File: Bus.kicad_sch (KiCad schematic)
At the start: 8 parts, among them X1.1 BUS_EC1834_16Bit, X1.2 BUS_EC1834_16Bit, X1.3 BUS_EC1834_16Bit, X1.4 BUS_EC1834_16Bit, X1.5 BUS_EC1834_16Bit, X1.6 BUS_EC1834_16Bit, X1.7 BUS_EC1834_16Bit, X1.8 BUS_EC1834_16Bit

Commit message: Completed BUS Final checks required
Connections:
- net GND: now reaches X1.2.a1 (GND)
- net GND: now also X1.1.a1 (GND), X1.1.a10 (GND), X1.1.a31 (GND), X1.1.a32 (GND), X1.2.a10 (GND), X1.2.a31 (GND), X1.2.a32 (GND), X1.3.a1 (GND), X1.3.a10 (GND), X1.3.a31 (GND), X1.3.a32 (GND), X1.4.a1 (GND), X1.4.a10 (GND), X1.4.a31 (GND), X1.4.a32 (GND), X1.5.a1 (GND), X1.5.a10 (GND), X1.5.a31 (GND), X1.5.a32 (GND), X1.6.a1 (GND), X1.6.a10 (GND), X1.6.a31 (GND), X1.6.a32 (GND), X1.7.a1 (GND), X1.7.a10 (GND), X1.7.a31 (GND), X1.7.a32 (GND), X1.8.a1 (GND), X1.8.a10 (GND), X1.8.a31 (GND), X1.8.a32 (GND)
- net ~{MEMW}: now reaches X1.2.a11 (~{MEMW})
- net ~{MEMW}: now also X1.1.a11 (~{MEMW}), X1.3.a11 (~{MEMW}), X1.4.a11 (~{MEMW}), X1.5.a11 (~{MEMW}), X1.6.a11 (~{MEMW}), X1.7.a11 (~{MEMW}), X1.8.a11 (~{MEMW})
- net ~{MEMR}: now reaches X1.2.a12 (~{MEMR})
- net ~{MEMR}: now also X1.1.a12 (~{MEMR}), X1.3.a12 (~{MEMR}), X1.4.a12 (~{MEMR}), X1.5.a12 (~{MEMR}), X1.6.a12 (~{MEMR}), X1.7.a12 (~{MEMR}), X1.8.a12 (~{MEMR})
- net ~{IOW}: now reaches X1.2.a13 (~{IOW})
- net ~{IOW}: now also X1.1.a13 (~{IOW}), X1.3.a13 (~{IOW}), X1.4.a13 (~{IOW}), X1.5.a13 (~{IOW}), X1.6.a13 (~{IOW}), X1.7.a13 (~{IOW}), X1.8.a13 (~{IOW})
- net ~{IOR}: now reaches X1.2.a14 (~{IOR})
- net ~{IOR}: now also X1.1.a14 (~{IOR}), X1.3.a14 (~{IOR}), X1.4.a14 (~{IOR}), X1.5.a14 (~{IOR}), X1.6.a14 (~{IOR}), X1.7.a14 (~{IOR}), X1.8.a14 (~{IOR})
- net ~{DACK3}: now reaches X1.2.a15 (~{DACK3})
- net ~{DACK3}: now also X1.1.a15 (~{DACK3}), X1.3.a15 (~{DACK3}), X1.4.a15 (~{DACK3}), X1.5.a15 (~{DACK3}), X1.6.a15 (~{DACK3}), X1.7.a15 (~{DACK3}), X1.8.a15 (~{DACK3})
- net DRQ3: now reaches X1.2.a16 (DRQ3)
- net DRQ3: now also X1.1.a16 (DRQ3), X1.3.a16 (DRQ3), X1.4.a16 (DRQ3), X1.5.a16 (DRQ3), X1.6.a16 (DRQ3), X1.7.a16 (DRQ3), X1.8.a16 (DRQ3)
- net ~{DACK1}: now reaches X1.2.a17 (~{DACK1})
- net ~{DACK1}: now also X1.1.a17 (~{DACK1}), X1.3.a17 (~{DACK1}), X1.4.a17 (~{DACK1}), X1.5.a17 (~{DACK1}), X1.6.a17 (~{DACK1}), X1.7.a17 (~{DACK1}), X1.8.a17 (~{DACK1})
- net DRQ1: now reaches X1.2.a18 (DRQ1)
- net DRQ1: now also X1.1.a18 (DRQ1), X1.3.a18 (DRQ1), X1.4.a18 (DRQ1), X1.5.a18 (DRQ1), X1.6.a18 (DRQ1), X1.7.a18 (DRQ1), X1.8.a18 (DRQ1)
- net ~{DACK0}: now reaches X1.2.a19 (~{DACK0})
- net ~{DACK0}: now also X1.1.a19 (~{DACK0}), X1.3.a19 (~{DACK0}), X1.4.a19 (~{DACK0}), X1.5.a19 (~{DACK0}), X1.6.a19 (~{DACK0}), X1.7.a19 (~{DACK0}), X1.8.a19 (~{DACK0})
- net RESET: now reaches X1.2.a2 (RESET)
- net RESET: now also X1.1.a2 (RESET), X1.3.a2 (RESET), X1.4.a2 (RESET), X1.5.a2 (RESET), X1.6.a2 (RESET), X1.7.a2 (RESET), X1.8.a2 (RESET)
- net CLK: now reaches X1.2.a20 (CLK)
- net CLK: now also X1.1.a20 (CLK), X1.3.a20 (CLK), X1.4.a20 (CLK), X1.5.a20 (CLK), X1.6.a20 (CLK), X1.7.a20 (CLK), X1.8.a20 (CLK)
- net IRQ7: now reaches X1.2.a21 (IRQ7)
- net IRQ7: now also X1.1.a21 (IRQ7), X1.3.a21 (IRQ7), X1.4.a21 (IRQ7), X1.5.a21 (IRQ7), X1.6.a21 (IRQ7), X1.7.a21 (IRQ7), X1.8.a21 (IRQ7)
- net IRQ6: now reaches X1.2.a22 (IRQ6)
- net IRQ6: now also X1.1.a22 (IRQ6), X1.3.a22 (IRQ6), X1.4.a22 (IRQ6), X1.5.a22 (IRQ6), X1.6.a22 (IRQ6), X1.7.a22 (IRQ6), X1.8.a22 (IRQ6)
- net IRQ5: now reaches X1.2.a23 (IRQ5)
- net IRQ5: now also X1.1.a23 (IRQ5), X1.3.a23 (IRQ5), X1.4.a23 (IRQ5), X1.5.a23 (IRQ5), X1.6.a23 (IRQ5), X1.7.a23 (IRQ5), X1.8.a23 (IRQ5)
- net IRQ4: now reaches X1.2.a24 (IRQ4)
- net IRQ4: now also X1.1.a24 (IRQ4), X1.3.a24 (IRQ4), X1.4.a24 (IRQ4), X1.5.a24 (IRQ4), X1.6.a24 (IRQ4), X1.7.a24 (IRQ4), X1.8.a24 (IRQ4)
- net IRQ3: now reaches X1.2.a25 (IRQ3)
- net IRQ3: now also X1.1.a25 (IRQ3), X1.3.a25 (IRQ3), X1.4.a25 (IRQ3), X1.5.a25 (IRQ3), X1.6.a25 (IRQ3), X1.7.a25 (IRQ3), X1.8.a25 (IRQ3)
- net ~{DACK2}: now reaches X1.2.a26 (~{DACK2})
- net ~{DACK2}: now also X1.1.a26 (~{DACK2}), X1.3.a26 (~{DACK2}), X1.4.a26 (~{DACK2}), X1.5.a26 (~{DACK2}), X1.6.a26 (~{DACK2}), X1.7.a26 (~{DACK2}), X1.8.a26 (~{DACK2})
- net TC: now reaches X1.2.a27 (TC)
- net TC: now also X1.1.a27 (TC), X1.3.a27 (TC), X1.4.a27 (TC), X1.5.a27 (TC), X1.6.a27 (TC), X1.7.a27 (TC), X1.8.a27 (TC)
- net ALE: now reaches X1.2.a28 (ALE)
- net ALE: now also X1.1.a28 (ALE), X1.3.a28 (ALE), X1.4.a28 (ALE), X1.5.a28 (ALE), X1.6.a28 (ALE), X1.7.a28 (ALE), X1.8.a28 (ALE)
- net +5V: now reaches X1.2.a29 (VCC)
- net +5V: now also X1.1.a29 (VCC), X1.1.a3 (+5V), X1.1.b30 (+5V), X1.2.a3 (+5V), X1.2.b30 (+5V), X1.3.a29 (VCC), X1.3.a3 (+5V), X1.3.b30 (+5V), X1.4.a29 (VCC), X1.4.a3 (+5V), X1.4.b30 (+5V), X1.5.a29 (VCC), X1.5.a3 (+5V), X1.5.b30 (+5V), X1.6.a29 (VCC), X1.6.a3 (+5V), X1.6.b30 (+5V), X1.7.a29 (VCC), X1.7.a3 (+5V), X1.7.b30 (+5V), X1.8.a29 (VCC), X1.8.a3 (+5V), X1.8.b30 (+5V)
- net OSC: now reaches X1.2.a30 (OSC)
- net OSC: now also X1.1.a30 (OSC), X1.3.a30 (OSC), X1.4.a30 (OSC), X1.5.a30 (OSC), X1.6.a30 (OSC), X1.7.a30 (OSC), X1.8.a30 (OSC)
- net IRQ2: now reaches X1.2.a4 (IRQ2)
- net IRQ2: now also X1.1.a4 (IRQ2), X1.3.a4 (IRQ2), X1.4.a4 (IRQ2), X1.5.a4 (IRQ2), X1.6.a4 (IRQ2), X1.7.a4 (IRQ2), X1.8.a4 (IRQ2)
- net -5V: now reaches X1.2.a5 (-5V)
- net -5V: now also X1.1.a5 (-5V), X1.3.a5 (-5V), X1.4.a5 (-5V), X1.5.a5 (-5V), X1.6.a5 (-5V), X1.7.a5 (-5V), X1.8.a5 (-5V)
- net DRQ2: now reaches X1.2.a6 (DRQ2)
- net DRQ2: now also X1.1.a6 (DRQ2), X1.3.a6 (DRQ2), X1.4.a6 (DRQ2), X1.5.a6 (DRQ2), X1.6.a6 (DRQ2), X1.7.a6 (DRQ2), X1.8.a6 (DRQ2)
- net -12V: now reaches X1.2.a7 (-12V)
- net -12V: now also X1.1.a7 (-12V), X1.3.a7 (-12V), X1.4.a7 (-12V), X1.5.a7 (-12V), X1.6.a7 (-12V), X1.7.a7 (-12V), X1.8.a7 (-12V)
- net +12V: now reaches X1.2.a9 (+12V)
- net +12V: now also X1.1.a9 (+12V), X1.3.a9 (+12V), X1.4.a9 (+12V), X1.5.a9 (+12V), X1.6.a9 (+12V), X1.7.a9 (+12V), X1.8.a9 (+12V)
- net DRQ0: now reaches X1.2.b19 (DRQ0)
- net DRQ0: now also X1.1.b19 (DRQ0), X1.3.b19 (DRQ0), X1.4.b19 (DRQ0), X1.5.b19 (DRQ0), X1.6.b19 (DRQ0), X1.7.b19 (DRQ0), X1.8.b19 (DRQ0)
- net IRQ10: now reaches X1.2.b21 (IRQ10)
- net IRQ10: now also X1.1.b21 (IRQ10), X1.3.b21 (IRQ10), X1.4.b21 (IRQ10), X1.5.b21 (IRQ10), X1.6.b21 (IRQ10), X1.7.b21 (IRQ10), X1.8.b21 (IRQ10)
- net IRQ11: now reaches X1.2.b22 (IRQ11)
- net IRQ11: now also X1.1.b22 (IRQ11), X1.3.b22 (IRQ11), X1.4.b22 (IRQ11), X1.5.b22 (IRQ11), X1.6.b22 (IRQ11), X1.7.b22 (IRQ11), X1.8.b22 (IRQ11)
- net IRQ12: now reaches X1.2.b23 (IRQ12)
- net IRQ12: now also X1.1.b23 (IRQ12), X1.3.b23 (IRQ12), X1.4.b23 (IRQ12), X1.5.b23 (IRQ12), X1.6.b23 (IRQ12), X1.7.b23 (IRQ12), X1.8.b23 (IRQ12)
- net IRQ15: now reaches X1.2.b24 (IRQ15)
- net IRQ15: now also X1.1.b24 (IRQ15), X1.3.b24 (IRQ15), X1.4.b24 (IRQ15), X1.5.b24 (IRQ15), X1.6.b24 (IRQ15), X1.7.b24 (IRQ15), X1.8.b24 (IRQ15)
- net IRQ14: now reaches X1.2.b25 (IRQ14)
- net IRQ14: now also X1.1.b25 (IRQ14), X1.3.b25 (IRQ14), X1.4.b25 (IRQ14), X1.5.b25 (IRQ14), X1.6.b25 (IRQ14), X1.7.b25 (IRQ14), X1.8.b25 (IRQ14)
- net ~{MASTER}: now reaches X1.2.b26 (~{MASTER})
- net ~{MASTER}: now also X1.1.b26 (~{MASTER}), X1.3.b26 (~{MASTER}), X1.4.b26 (~{MASTER}), X1.5.b26 (~{MASTER}), X1.6.b26 (~{MASTER}), X1.7.b26 (~{MASTER}), X1.8.b26 (~{MASTER})
- net ~{MEMCS16}: now reaches X1.2.b32 (~{MEMCS16})
- net ~{MEMCS16}: now also X1.1.b32 (~{MEMCS16}), X1.3.b32 (~{MEMCS16}), X1.4.b32 (~{MEMCS16}), X1.5.b32 (~{MEMCS16}), X1.6.b32 (~{MEMCS16}), X1.7.b32 (~{MEMCS16}), X1.8.b32 (~{MEMCS16})
- net ~{IOCHCK}: now reaches X1.2.c1 (~{IOCHCK})
- net ~{IOCHCK}: now also X1.1.c1 (~{IOCHCK}), X1.3.c1 (~{IOCHCK}), X1.4.c1 (~{IOCHCK}), X1.5.c1 (~{IOCHCK}), X1.6.c1 (~{IOCHCK}), X1.7.c1 (~{IOCHCK}), X1.8.c1 (~{IOCHCK})
- net IOCHRDY: now reaches X1.2.c10 (IOCHRDY)
- net IOCHRDY: now also X1.1.c10 (IOCHRDY), X1.3.c10 (IOCHRDY), X1.4.c10 (IOCHRDY), X1.5.c10 (IOCHRDY), X1.6.c10 (IOCHRDY), X1.7.c10 (IOCHRDY), X1.8.c10 (IOCHRDY)
- net AEN: now reaches X1.2.c11 (AEN)
- net AEN: now also X1.1.c11 (AEN), X1.3.c11 (AEN), X1.4.c11 (AEN), X1.5.c11 (AEN), X1.6.c11 (AEN), X1.7.c11 (AEN), X1.8.c11 (AEN)
- net A19: now reaches X1.2.c12 (BA19)
- net A19: now also X1.1.c12 (BA19), X1.4.c12 (BA19), X1.5.c12 (BA19), X1.6.c12 (BA19), X1.7.c12 (BA19), X1.8.c12 (BA19)
- net A18: now reaches X1.2.c13 (BA18)
- net A18: now also X1.1.c13 (BA18), X1.4.c13 (BA18), X1.5.c13 (BA18), X1.6.c13 (BA18), X1.7.c13 (BA18), X1.8.c13 (BA18)
- net A17: now reaches X1.2.c14 (BA17)
- net A17: now also X1.1.c14 (BA17), X1.4.c14 (BA17), X1.5.c14 (BA17), X1.6.c14 (BA17), X1.7.c14 (BA17), X1.8.c14 (BA17)
- net A16: now reaches X1.2.c15 (BA16)
- net A16: now also X1.1.c15 (BA16), X1.4.c15 (BA16), X1.5.c15 (BA16), X1.6.c15 (BA16), X1.7.c15 (BA16), X1.8.c15 (BA16)
- net A15: now reaches X1.2.c16 (BA15)
- net A15: now also X1.1.c16 (BA15), X1.4.c16 (BA15), X1.5.c16 (BA15), X1.6.c16 (BA15), X1.7.c16 (BA15), X1.8.c16 (BA15)
- net A14: now reaches X1.2.c17 (BA14)
- net A14: now also X1.1.c17 (BA14), X1.4.c17 (BA14), X1.5.c17 (BA14), X1.6.c17 (BA14), X1.7.c17 (BA14), X1.8.c17 (BA14)
- net A13: now reaches X1.2.c18 (BA13)
- net A13: now also X1.1.c18 (BA13), X1.4.c18 (BA13), X1.5.c18 (BA13), X1.6.c18 (BA13), X1.7.c18 (BA13), X1.8.c18 (BA13)
- net A12: now reaches X1.2.c19 (BA12)
- net A12: now also X1.1.c19 (BA12), X1.4.c19 (BA12), X1.5.c19 (BA12), X1.6.c19 (BA12), X1.7.c19 (BA12), X1.8.c19 (BA12)
- net D7: now reaches X1.2.c2 (DB7)
- net D7: now also X1.1.c2 (DB7), X1.3.c2 (DB7), X1.4.c2 (DB7), X1.5.c2 (DB7), X1.7.c2 (DB7), X1.8.c2 (DB7)
- net A11: now reaches X1.2.c20 (BA11)
- net A11: now also X1.1.c20 (BA11), X1.4.c20 (BA11), X1.5.c20 (BA11), X1.6.c20 (BA11), X1.7.c20 (BA11), X1.8.c20 (BA11)
- net A10: now reaches X1.2.c21 (BA10)
- net A10: now also X1.1.c21 (BA10), X1.4.c21 (BA10), X1.5.c21 (BA10), X1.6.c21 (BA10), X1.7.c21 (BA10), X1.8.c21 (BA10)
- net A9: now reaches X1.2.c22 (BA09)
- net A9: now also X1.1.c22 (BA09), X1.4.c22 (BA09), X1.5.c22 (BA09), X1.6.c22 (BA09), X1.7.c22 (BA09), X1.8.c22 (BA09)
- net A8: now reaches X1.2.c23 (BA08)
- net A8: now also X1.1.c23 (BA08), X1.4.c23 (BA08), X1.5.c23 (BA08), X1.6.c23 (BA08), X1.7.c23 (BA08), X1.8.c23 (BA08)
- net A7: now reaches X1.2.c24 (BA07)
- net A7: now also X1.1.c24 (BA07), X1.4.c24 (BA07), X1.5.c24 (BA07), X1.6.c24 (BA07), X1.7.c24 (BA07), X1.8.c24 (BA07)
- net A6: now reaches X1.2.c25 (BA06)
- net A6: now also X1.1.c25 (BA06), X1.4.c25 (BA06), X1.5.c25 (BA06), X1.6.c25 (BA06), X1.7.c25 (BA06), X1.8.c25 (BA06)
- net A5: now reaches X1.2.c26 (BA05)
- net A5: now also X1.1.c26 (BA05), X1.4.c26 (BA05), X1.5.c26 (BA05), X1.6.c26 (BA05), X1.7.c26 (BA05), X1.8.c26 (BA05)
- net A4: now reaches X1.2.c27 (BA04)
- net A4: now also X1.1.c27 (BA04), X1.4.c27 (BA04), X1.5.c27 (BA04), X1.6.c27 (BA04), X1.7.c27 (BA04), X1.8.c27 (BA04)
- net A3: now reaches X1.2.c28 (BA03)
- net A3: now also X1.1.c28 (BA03), X1.4.c28 (BA03), X1.5.c28 (BA03), X1.6.c28 (BA03), X1.7.c28 (BA03), X1.8.c28 (BA03)
- net A2: now reaches X1.2.c29 (BA02)
- net A2: now also X1.1.c29 (BA02), X1.4.c29 (BA02), X1.5.c29 (BA02), X1.6.c29 (BA02), X1.7.c29 (BA02), X1.8.c29 (BA02)
- net D6: now reaches X1.2.c3 (DB6)
- net D6: now also X1.1.c3 (DB6), X1.3.c3 (DB6), X1.4.c3 (DB6), X1.5.c3 (DB6), X1.7.c3 (DB6), X1.8.c3 (DB6)
- net A1: now reaches X1.2.c30 (BA01)
- net A1: now also X1.1.c30 (BA01), X1.4.c30 (BA01), X1.5.c30 (BA01), X1.6.c30 (BA01), X1.7.c30 (BA01), X1.8.c30 (BA01)
- net A0: now reaches X1.2.c31 (BA00)
- net A0: now also X1.1.c31 (BA00), X1.4.c31 (BA00), X1.5.c31 (BA00), X1.6.c31 (BA00), X1.7.c31 (BA00), X1.8.c31 (BA00)
- net ~{BHE}: now reaches X1.2.c32 (~{BHE})
- net ~{BHE}: now also X1.1.c32 (~{BHE}), X1.3.c32 (~{BHE}), X1.4.c32 (~{BHE}), X1.5.c32 (~{BHE}), X1.6.c32 (~{BHE}), X1.7.c32 (~{BHE}), X1.8.c32 (~{BHE})
- net D5: now reaches X1.2.c4 (DB5)
- net D5: now also X1.1.c4 (DB5), X1.3.c4 (DB5), X1.4.c4 (DB5), X1.5.c4 (DB5), X1.7.c4 (DB5), X1.8.c4 (DB5)
- net D4: now reaches X1.2.c5 (DB4)
- net D4: now also X1.1.c5 (DB4), X1.3.c5 (DB4), X1.4.c5 (DB4), X1.5.c5 (DB4), X1.6.c5 (DB4), X1.7.c5 (DB4), X1.8.c5 (DB4)
- net D3: now reaches X1.2.c6 (DB3)
- net D3: now also X1.1.c6 (DB3), X1.3.c6 (DB3), X1.4.c6 (DB3), X1.5.c6 (DB3), X1.6.c6 (DB3), X1.7.c6 (DB3), X1.8.c6 (DB3)
- net D2: now reaches X1.2.c7 (DB2)
- net D2: now also X1.1.c7 (DB2), X1.3.c7 (DB2), X1.4.c7 (DB2), X1.5.c7 (DB2), X1.6.c7 (DB2), X1.7.c7 (DB2), X1.8.c7 (DB2)
- net D1: now reaches X1.2.c8 (DB1)
- net D1: now also X1.1.c8 (DB1), X1.3.c8 (DB1), X1.4.c8 (DB1), X1.5.c8 (DB1), X1.6.c8 (DB1), X1.7.c8 (DB1), X1.8.c8 (DB1)
- net D0: now reaches X1.2.c9 (DB0)
- net D0: now also X1.1.c9 (DB0), X1.3.c9 (DB0), X1.4.c9 (DB0), X1.5.c9 (DB0), X1.6.c9 (DB0), X1.7.c9 (DB0), X1.8.c9 (DB0)
- no-connect marks 0 -> 8
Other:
- company: (none) -> Mario Gögel 2022
- title: (none) -> EC1834 Hauptplatine 201.1-BUS
- moved on the sheet: X1.1, X1.2, X1.3, X1.4, X1.5, X1.6, X1.7, X1.8

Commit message: Modifications to pass most ERC checks modified symbols for ERC check Added some notes
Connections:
- net A0: now also X1.3.c31 (BA00)
- net A1: now also X1.3.c30 (BA01)
- net A10: now also X1.3.c21 (BA10)
- net A11: now also X1.3.c20 (BA11)
- net A12: now also X1.3.c19 (BA12)
- net A13: now also X1.3.c18 (BA13)
- net A14: now also X1.3.c17 (BA14)
- net A15: now also X1.3.c16 (BA15)
- net A16: now also X1.3.c15 (BA16)
- net A17: now also X1.3.c14 (BA17)
- net A18: now also X1.3.c13 (BA18)
- net A19: now also X1.3.c12 (BA19)
- net A2: now also X1.3.c29 (BA02)
- net A3: now also X1.3.c28 (BA03)
- net A4: now also X1.3.c27 (BA04)
- net A5: now also X1.3.c26 (BA05)
- net A6: now also X1.3.c25 (BA06)
- net A7: now also X1.3.c24 (BA07)
- net A8: now also X1.3.c23 (BA08)
- net A9: now also X1.3.c22 (BA09)
- net D5: now also X1.6.c4 (DB5)
- net D6: now also X1.6.c3 (DB6)
- net D7: now also X1.6.c2 (DB7)

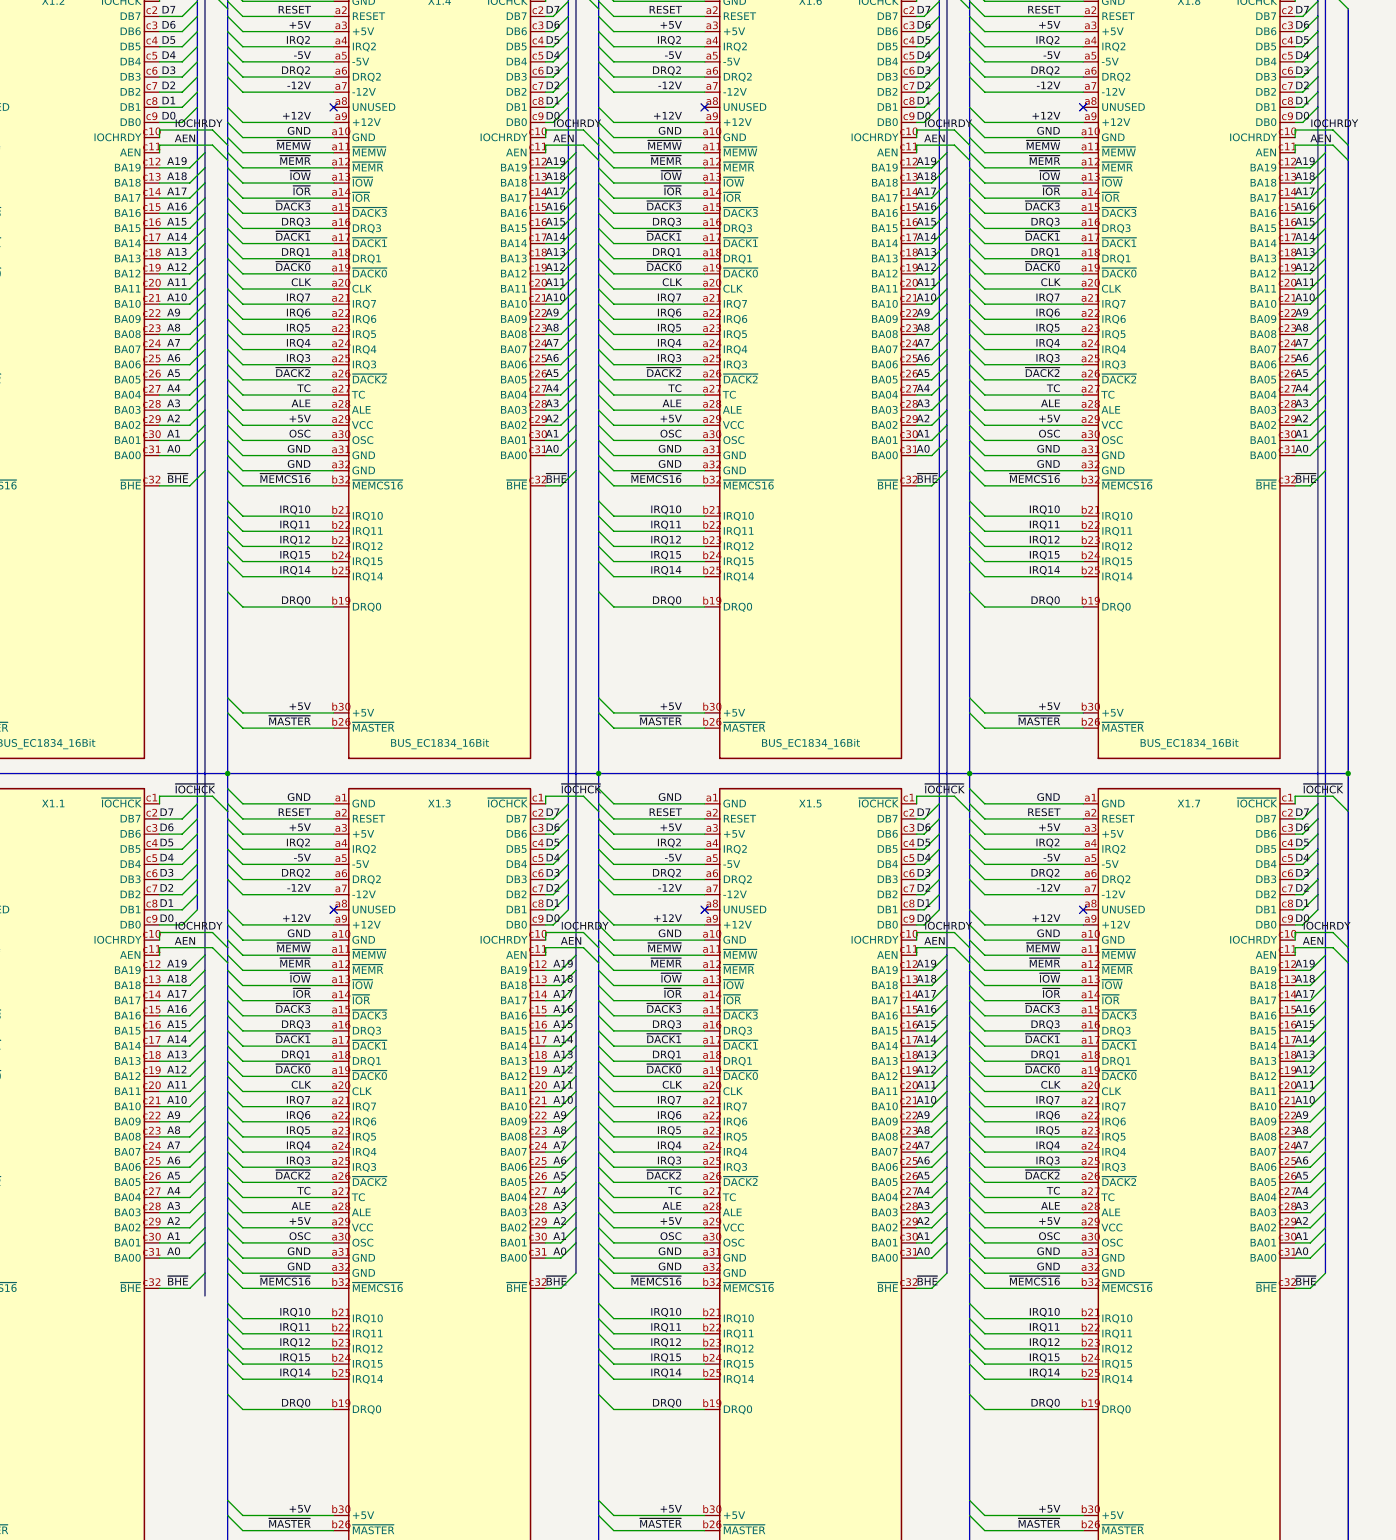
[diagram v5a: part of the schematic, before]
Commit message: Updated ec1834 symbols Fixed missing D8-D15 on bus connector Updated PDFs
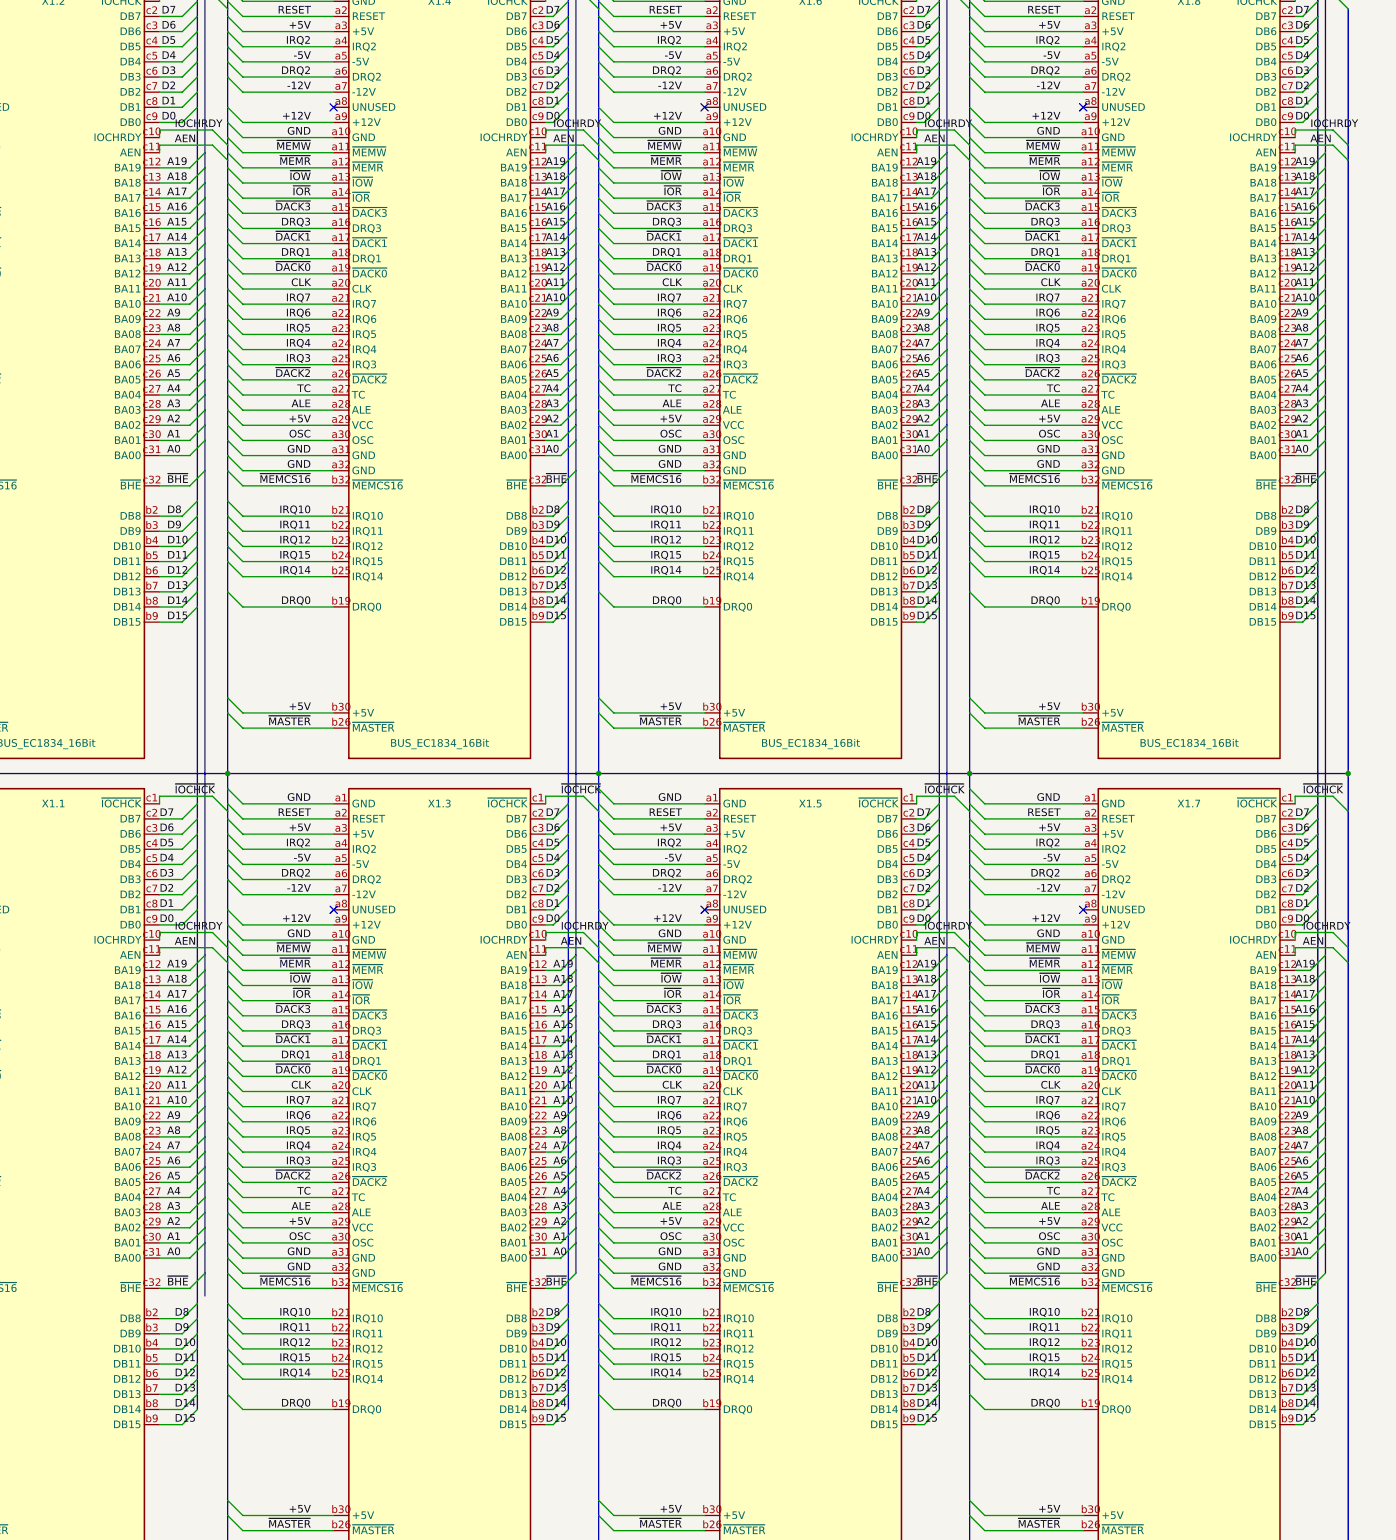
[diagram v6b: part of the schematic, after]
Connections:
- new net D10: X1.1.b4 (DB10), X1.2.b4 (DB10), X1.3.b4 (DB10), X1.4.b4 (DB10), X1.5.b4 (DB10), X1.6.b4 (DB10), X1.7.b4 (DB10), X1.8.b4 (DB10)
- new net D11: X1.1.b5 (DB11), X1.2.b5 (DB11), X1.3.b5 (DB11), X1.4.b5 (DB11), X1.5.b5 (DB11), X1.6.b5 (DB11), X1.7.b5 (DB11), X1.8.b5 (DB11)
- new net D12: X1.1.b6 (DB12), X1.2.b6 (DB12), X1.3.b6 (DB12), X1.4.b6 (DB12), X1.5.b6 (DB12), X1.6.b6 (DB12), X1.7.b6 (DB12), X1.8.b6 (DB12)
- new net D13: X1.1.b7 (DB13), X1.2.b7 (DB13), X1.3.b7 (DB13), X1.4.b7 (DB13), X1.5.b7 (DB13), X1.6.b7 (DB13), X1.7.b7 (DB13), X1.8.b7 (DB13)
- new net D14: X1.1.b8 (DB14), X1.2.b8 (DB14), X1.3.b8 (DB14), X1.4.b8 (DB14), X1.5.b8 (DB14), X1.6.b8 (DB14), X1.7.b8 (DB14), X1.8.b8 (DB14)
- new net D15: X1.1.b9 (DB15), X1.2.b9 (DB15), X1.3.b9 (DB15), X1.4.b9 (DB15), X1.5.b9 (DB15), X1.6.b9 (DB15), X1.7.b9 (DB15), X1.8.b9 (DB15)
- new net D8: X1.1.b2 (DB8), X1.2.b2 (DB8), X1.3.b2 (DB8), X1.4.b2 (DB8), X1.5.b2 (DB8), X1.6.b2 (DB8), X1.7.b2 (DB8), X1.8.b2 (DB8)
- new net D9: X1.1.b3 (DB9), X1.2.b3 (DB9), X1.3.b3 (DB9), X1.4.b3 (DB9), X1.5.b3 (DB9), X1.6.b3 (DB9), X1.7.b3 (DB9), X1.8.b3 (DB9)
